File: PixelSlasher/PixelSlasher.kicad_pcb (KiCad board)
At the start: 2 copper layers, 52.8 x 149.3 mm, 22 parts, among them J1 VGA Input, J2 CV Red, J3 CV Green, J4 CV Blue, Q1 BC337, Q2 BC337, Q3 BC337, SW1 SW_SPDT, SW2 SW_SPDT, SW3 SW_SPDT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

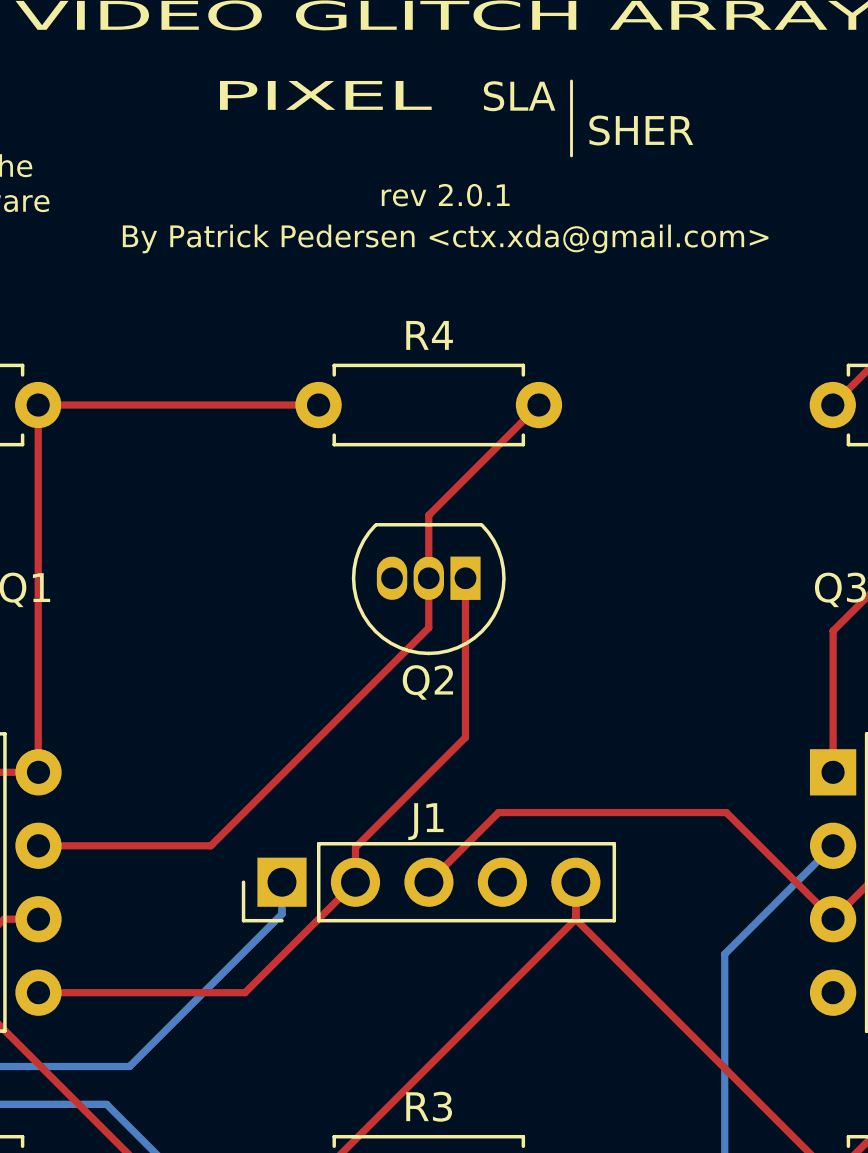
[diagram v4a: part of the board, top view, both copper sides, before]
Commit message: PixelSlasher: Rev 2.0.2: Set pin header labels to silk screen
Signed-off-by: Patrick Pedersen <ctx.xda@gmail.com>
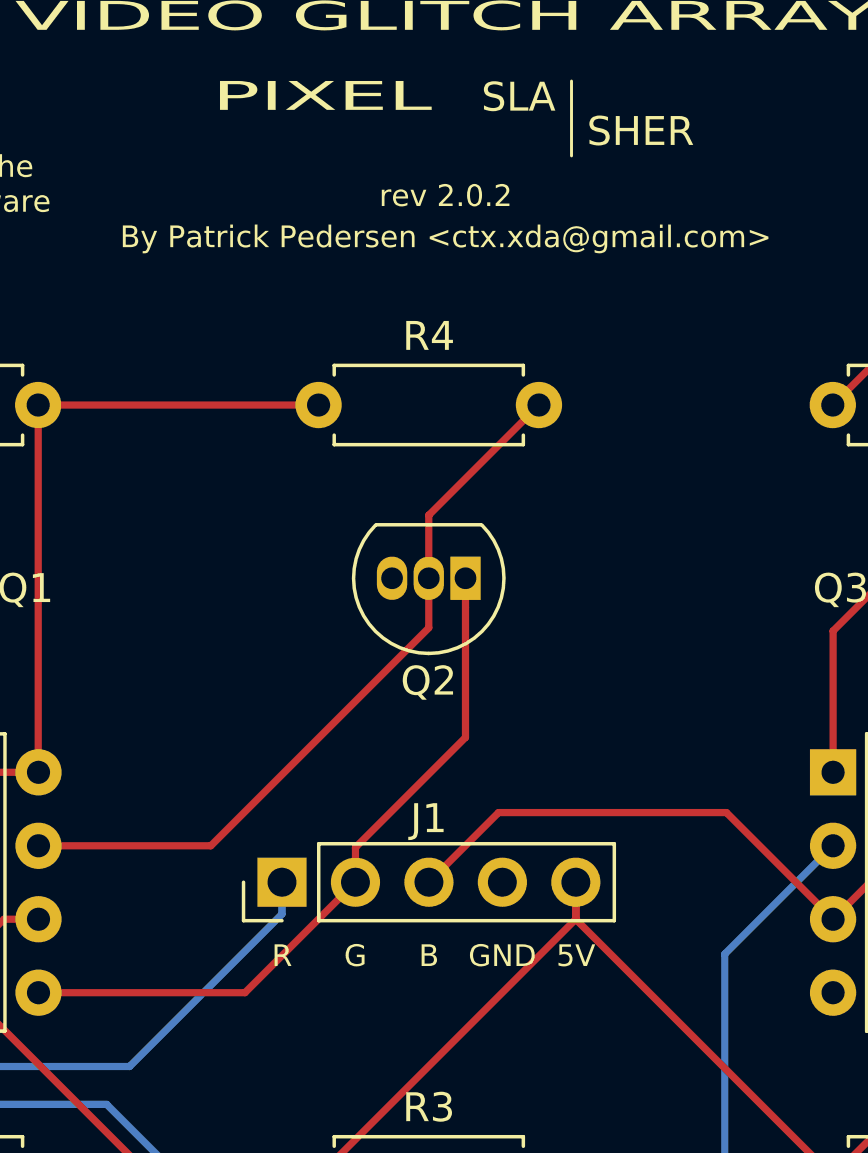
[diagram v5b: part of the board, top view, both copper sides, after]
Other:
- board text added: "rev 2.0.2"
- board text removed: "rev 2.0.1"
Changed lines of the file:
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@@
   (title_block
     (date 2019-08-30)
-    (rev 2.0.1)
+    (rev 2.0.2)
     (comment 2 https://www.tapr.org/ohl.html)
     (comment 3 "License: TAPR Open Hardware License v1.0")
@@
       (net 17 "Net-(J4-Pad1)"))
   )
-  (gr_text R (at 124.945 68.58) (layer F.CrtYd)
+  (gr_text R (at 124.945 68.58) (layer F.SilkS)
     (effects (font (size 0.75 0.75) (thickness 0.1)))
   )
-  (gr_text G (at 127.485 68.58) (layer F.CrtYd)
+  (gr_text G (at 127.485 68.58) (layer F.SilkS)
     (effects (font (size 0.75 0.75) (thickness 0.1)))
   )
-  (gr_text B (at 130.025 68.58) (layer F.CrtYd)
+  (gr_text B (at 130.025 68.58) (layer F.SilkS)
     (effects (font (size 0.75 0.75) (thickness 0.1)))
   )
-  (gr_text 5V (at 135.105 68.58) (layer F.CrtYd)
+  (gr_text 5V (at 135.105 68.58) (layer F.SilkS)
     (effects (font (size 0.75 0.75) (thickness 0.1)))
   )
-  (gr_text GND (at 132.565 68.58) (layer F.CrtYd)
+  (gr_text GND (at 132.565 68.58) (layer F.SilkS)
     (effects (font (size 0.75 0.75) (thickness 0.1)))
   )
@@
   (gr_circle (center 111.42 38.5826) (end 112.17 38.5826) (layer Edge.Cuts) (width 0.12))
   (gr_circle (center 149.9108 38.5826) (end 150.6608 38.5826) (layer Edge.Cuts) (width 0.12))
-  (gr_text "rev 2.0.1" (at 130.6068 42.30116) (layer F.SilkS)
+  (gr_text "rev 2.0.2" (at 130.6068 42.30116) (layer F.SilkS)
     (effects (font (size 0.75 0.75) (thickness 0.1)))
   )

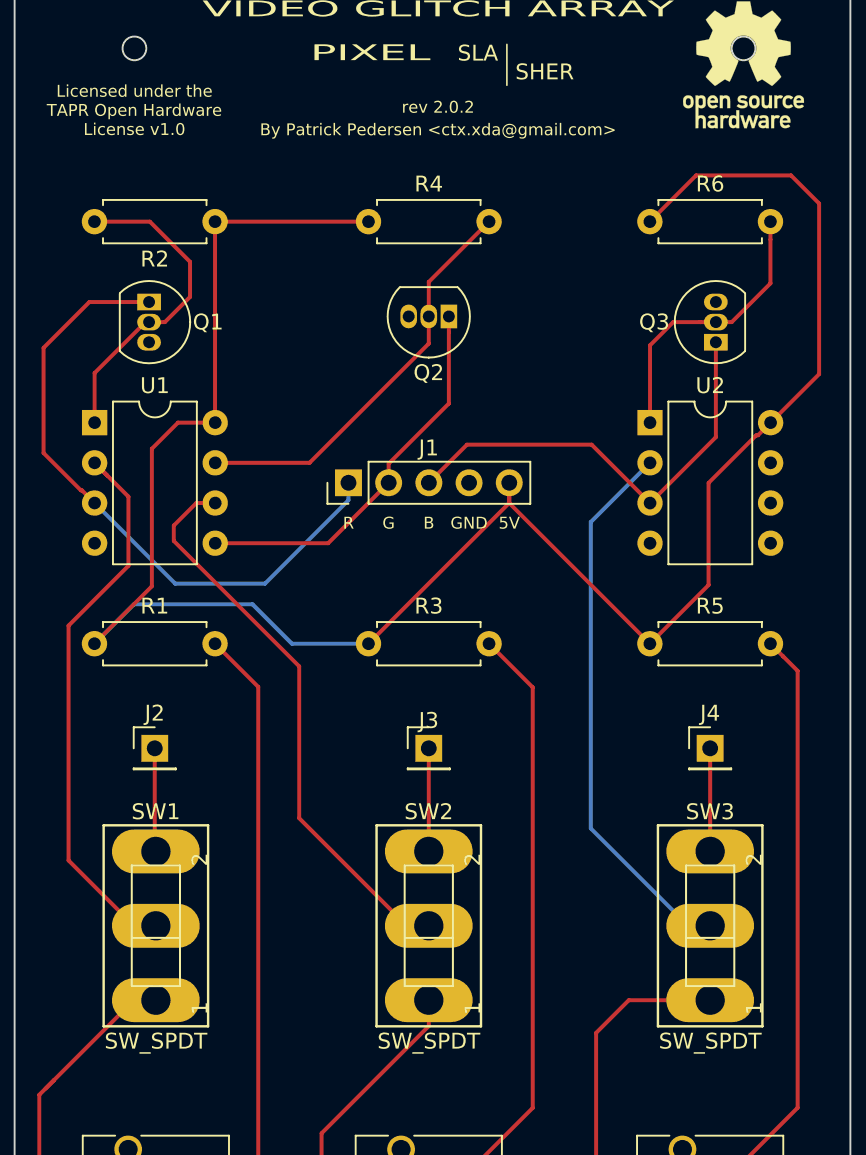
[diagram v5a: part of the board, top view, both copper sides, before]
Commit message: PixelSlasher: Rev 2.0.3: Fixed R2 ref designator + minor changes in distances for ref designators
Signed-off-by: Patrick Pedersen <ctx.xda@gmail.com>
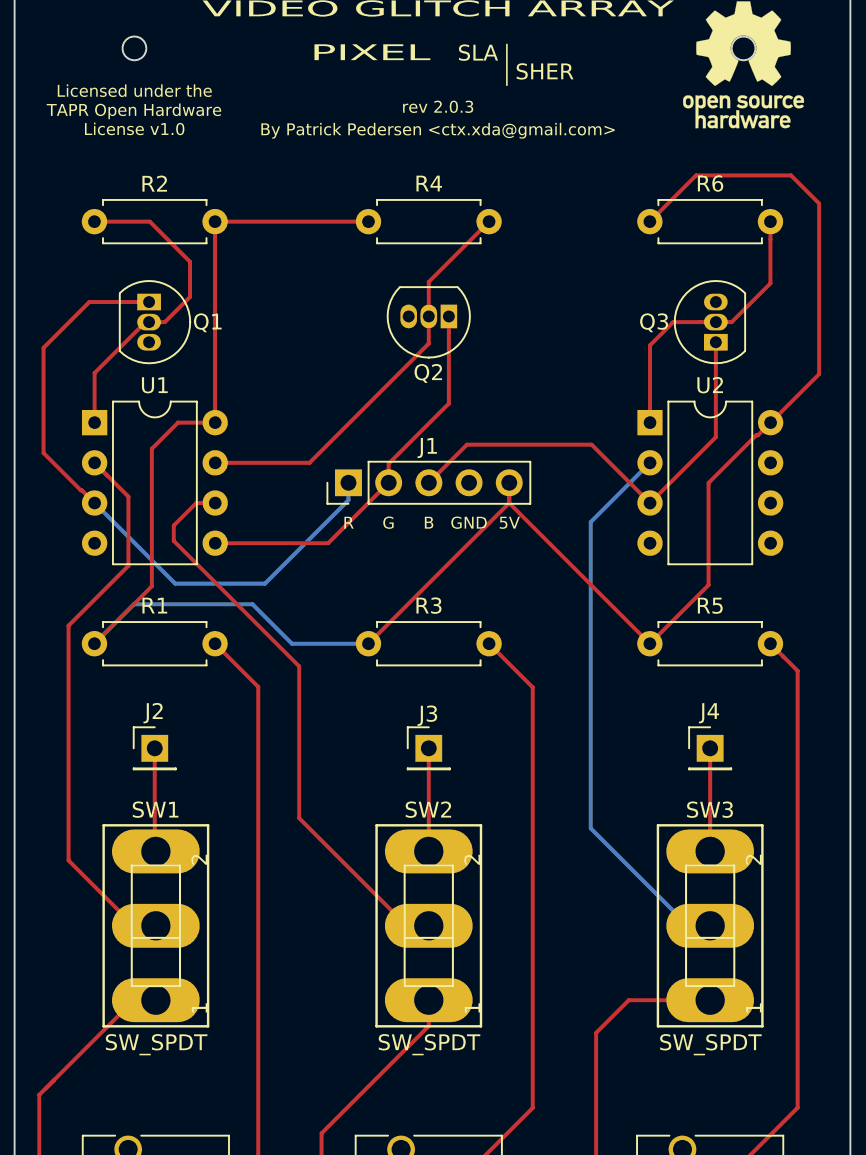
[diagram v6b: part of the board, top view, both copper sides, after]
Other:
- board text added: "rev 2.0.3"
- board text removed: "rev 2.0.2"
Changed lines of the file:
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@@
   (title_block
     (date 2019-08-30)
-    (rev 2.0.2)
+    (rev 2.0.3)
     (comment 2 https://www.tapr.org/ohl.html)
     (comment 3 "License: TAPR Open Hardware License v1.0")
@@
     (descr "Through hole straight pin header, 1x05, 2.54mm pitch, single row")
     (tags "Through hole pin header THT 1x05 2.54mm single row")
-    (fp_text reference J1 (at 2.195 5.075 180) (layer F.SilkS)
+    (fp_text reference J1 (at 2.295 5.075 180) (layer F.SilkS)
       (effects (font (size 1 1) (thickness 0.15)))
     )
@@
     (descr "Resistor, Axial_DIN0207 series, Axial, Horizontal, pin pitch=7.62mm, 0.25W = 1/4W, length*diameter=6.3*2.5mm^2, http://cdn-reichelt.de/documents/datenblatt/B400/1_4W%23YAG.pdf")
     (tags "Resistor Axial_DIN0207 series Axial Horizontal pin pitch 7.62mm 0.25W = 1/4W length 6.3mm diameter 2.5mm")
-    (fp_text reference R2 (at 3.81 -2.37) (layer F.SilkS)
+    (fp_text reference R2 (at 3.81 2.3558) (layer F.SilkS)
       (effects (font (size 1 1) (thickness 0.15)))
     )
@@
     (descr "Through hole straight pin header, 1x01, 2.54mm pitch, single row")
     (tags "Through hole pin header THT 1x01 2.54mm single row")
-    (fp_text reference J2 (at 0 -2.21364) (layer F.SilkS)
+    (fp_text reference J2 (at 0 -2.31364) (layer F.SilkS)
       (effects (font (size 1 1) (thickness 0.15)))
     )
@@
     (descr "Through hole straight pin header, 1x01, 2.54mm pitch, single row")
     (tags "Through hole pin header THT 1x01 2.54mm single row")
-    (fp_text reference J3 (at 0 -1.75288) (layer F.SilkS)
+    (fp_text reference J3 (at 0 -2.15288) (layer F.SilkS)
       (effects (font (size 1 1) (thickness 0.15)))
     )
@@
     (descr "Through hole straight pin header, 1x01, 2.54mm pitch, single row")
     (tags "Through hole pin header THT 1x01 2.54mm single row")
-    (fp_text reference J4 (at 0 -2.21516) (layer F.SilkS)
+    (fp_text reference J4 (at 0 -2.31516) (layer F.SilkS)
       (effects (font (size 1 1) (thickness 0.15)))
     )
@@
     (at 112.776 94.02572 90)
     (descr "<b>SLIDING SWITCH</b><p>distributor Buerklin, 11G810")
-    (fp_text reference SW1 (at 7.20372 0 180) (layer F.SilkS)
+    (fp_text reference SW1 (at 7.30372 0 180) (layer F.SilkS)
       (effects (font (size 1 1) (thickness 0.05)))
     )
-    (fp_text value SW_SPDT (at -7.29516 0 180) (layer F.SilkS)
+    (fp_text value SW_SPDT (at -7.39516 0 180) (layer F.SilkS)
       (effects (font (size 1 1) (thickness 0.05)))
     )
@@
     (at 130.02 94.02572 90)
     (descr "<b>SLIDING SWITCH</b><p>distributor Buerklin, 11G810")
-    (fp_text reference SW2 (at 7.20372 0 180) (layer F.SilkS)
+    (fp_text reference SW2 (at 7.30372 0 180) (layer F.SilkS)
       (effects (font (size 1 1) (thickness 0.05)))
     )
-    (fp_text value SW_SPDT (at -7.29516 0 180) (layer F.SilkS)
+    (fp_text value SW_SPDT (at -7.39516 0 180) (layer F.SilkS)
       (effects (font (size 1 1) (thickness 0.05)))
     )
@@
     (at 147.8 94.02572 90)
     (descr "<b>SLIDING SWITCH</b><p>distributor Buerklin, 11G810")
-    (fp_text reference SW3 (at 7.20118 0 180) (layer F.SilkS)
+    (fp_text reference SW3 (at 7.30118 0 180) (layer F.SilkS)
       (effects (font (size 1 1) (thickness 0.05)))
     )
-    (fp_text value SW_SPDT (at -7.29516 0 180) (layer F.SilkS)
+    (fp_text value SW_SPDT (at -7.39516 0 180) (layer F.SilkS)
       (effects (font (size 1 1) (thickness 0.05)))
     )
@@
   (gr_circle (center 111.42 38.5826) (end 112.17 38.5826) (layer Edge.Cuts) (width 0.12))
   (gr_circle (center 149.9108 38.5826) (end 150.6608 38.5826) (layer Edge.Cuts) (width 0.12))
-  (gr_text "rev 2.0.2" (at 130.6068 42.30116) (layer F.SilkS)
+  (gr_text "rev 2.0.3" (at 130.6068 42.30116) (layer F.SilkS)
     (effects (font (size 0.75 0.75) (thickness 0.1)))
   )

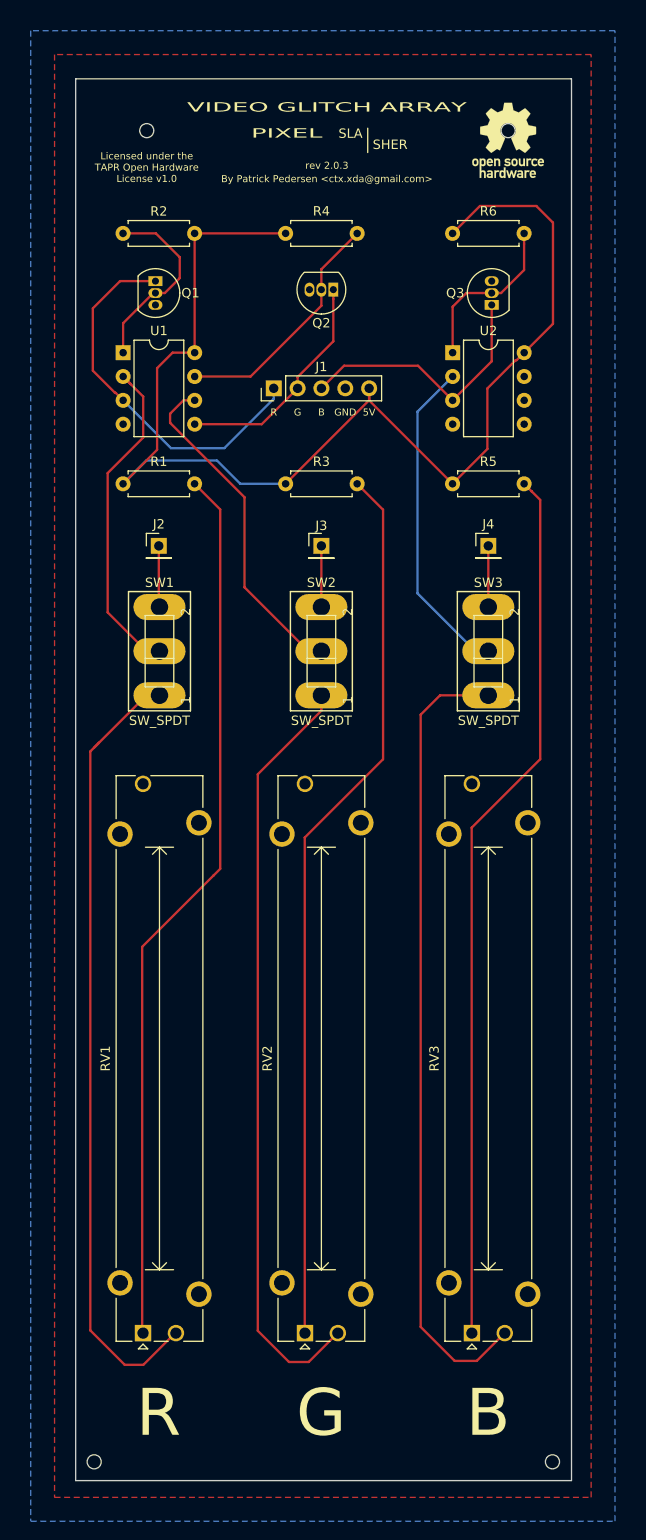
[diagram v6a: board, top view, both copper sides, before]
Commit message: PixelSlasher: Rev 2.0.4: Vertically centered CV/Pot switches
Signed-off-by: Patrick Pedersen <ctx.xda@gmail.com>
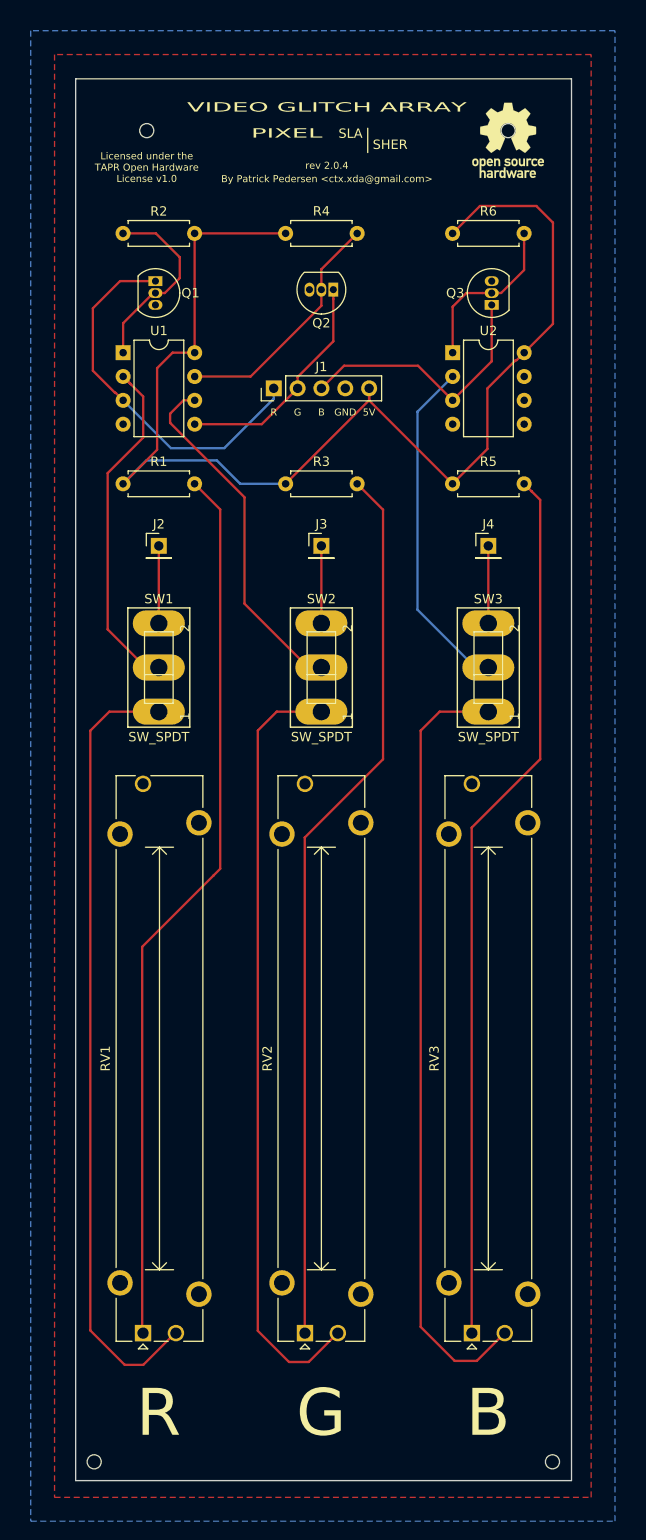
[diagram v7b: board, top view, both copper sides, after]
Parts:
- moved SW1 1.74 mm to (112.7, 95.8)
- moved SW2 1.74 mm to (130.0, 95.8)
- moved SW3 1.74 mm to (147.8, 95.8)
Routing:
- net Net-(SW3-Pad2): track 34.7 -> 36.5 mm
- net Net-(SW2-Pad2): track 36.0 -> 37.7 mm
- net Net-(J4-Pad1): track 6.52 -> 8.26 mm
- net Net-(J3-Pad1): track 6.52 -> 8.26 mm
- net Net-(RV3-Pad2): track 84.9 -> 83.2 mm
- net Net-(J2-Pad1): track 6.55 -> 8.26 mm
- net Net-(SW1-Pad2): track 35.9 -> 37.7 mm
- net Net-(RV2-Pad2): track 81.6 -> 82.7 mm
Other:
- board text added: "rev 2.0.4"
- board text removed: "rev 2.0.3"
